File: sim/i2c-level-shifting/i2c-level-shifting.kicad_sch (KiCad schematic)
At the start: 13 parts, among them Q1 NX6008NBKW

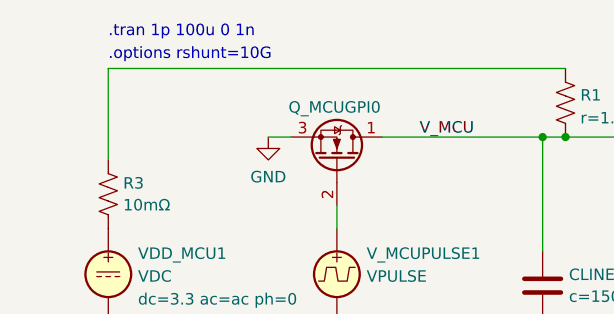
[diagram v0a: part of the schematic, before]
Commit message: More sane transient parameters.
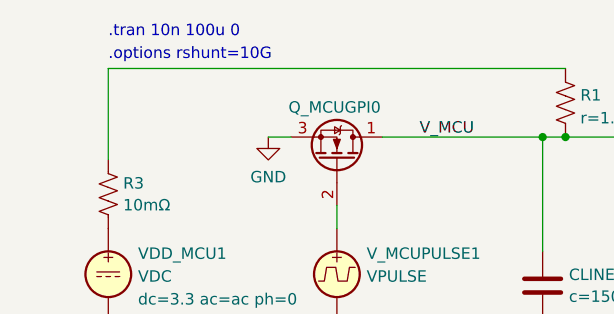
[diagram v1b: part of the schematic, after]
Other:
- note added: ".tran 10n 100u 0"
- note removed: ".tran 1p 100u 0 1n"
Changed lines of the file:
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@@
     (effects (font (size 1.27 1.27)) (justify left bottom))
   )
-  (text ".tran 1p 100u 0 1n" (at 76.2 123.698 0)
+  (text ".tran 10n 100u 0" (at 76.2 123.698 0)
     (effects (font (size 1.27 1.27)) (justify left bottom))
   )

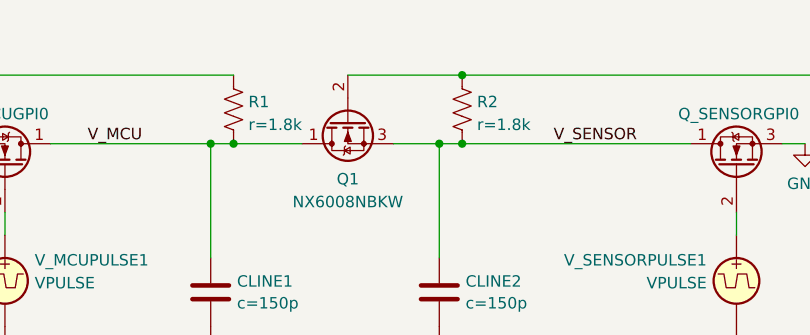
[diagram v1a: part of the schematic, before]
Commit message: Added gate resistors to reduce di/dt and thus supply noise.
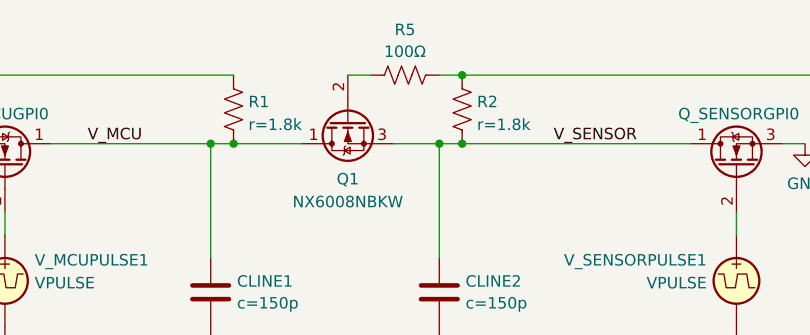
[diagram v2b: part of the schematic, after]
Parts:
- added R5: 100Ω, restall-generic-resistors:nominal-0402-1005, symbol restall-generic-resistors:resistor
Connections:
- net at R2.1, R4.1: now also R5.2; no longer Q1.2 (G)
- new net: Q1.2 (G), R5.1
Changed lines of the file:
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@@
     (stroke (width 0) (type default))
   )
-  (wire (pts (xy 139.7 127) (xy 152.4 127))
+  (wire (pts (xy 139.7 127) (xy 142.24 127))
     (stroke (width 0) (type default))
   )
@@
     (stroke (width 0) (type default))
   )
+  (wire (pts (xy 101.6 142.24) (xy 101.6 144.78))
+    (stroke (width 0) (type default))
+  )
   (wire (pts (xy 152.4 127) (xy 203.2 127))
     (stroke (width 0) (type default))
   )
-  (wire (pts (xy 101.6 142.24) (xy 101.6 144.78))
-    (stroke (width 0) (type default))
-  )
   (wire (pts (xy 124.46 134.62) (xy 124.46 147.32))
     (stroke (width 0) (type default))
   )
   (wire (pts (xy 73.66 193.04) (xy 68.58 193.04))
+    (stroke (width 0) (type default))
+  )
+  (wire (pts (xy 149.86 127) (xy 152.4 127))
     (stroke (width 0) (type default))
   )
@@
         )
       )
+    )
+  )
+  (symbol (lib_id "restall-generic-resistors:resistor") (at 146.05 127 90) (unit 1)
+    (in_bom yes) (on_board yes) (dnp no) (fields_autoplaced)
+    (property "Reference" "R5" (at 146.05 121.9667 90)
+      (effects (font (size 1.27 1.27)))
+    )
+    (property "Value" "100Ω" (at 146.05 124.3909 90)
+      (effects (font (size 1.27 1.27)))
+    )
+    (property "Footprint" "restall-generic-resistors:nominal-0402-1005" (at 146.304 125.984 90)
+      (effects (font (size 1.27 1.27)) (justify left) hide)
+    )
+    (property "Datasheet" "~" (at 146.05 127 0)
+      (effects (font (size 1.27 1.27)) (justify left) hide)
+    )
+    (property "Label" "???kΩ±1% ???W" (at 147.574 125.222 0)
+      (effects (font (size 1.27 1.27)) (justify left) hide)
+    )
+    (property "Tolerance" "±1%" (at 149.606 125.222 0)
+      (effects (font (size 1.27 1.27)) (justify left) hide)
+    )
+    (property "PowerRating" "0.0625W" (at 151.638 125.222 0)
+      (effects (font (size 1.27 1.27)) (justify left) hide)
+    )
+    (property "TemperatureCoefficient" "±100ppm" (at 153.67 125.222 0)
+      (effects (font (size 1.27 1.27)) (justify left) hide)
+    )
+    (property "Construction" "Thick Film" (at 155.702 125.222 0)
+      (effects (font (size 1.27 1.27)) (justify left) hide)
+    )
+    (property "Package" "0402" (at 157.734 125.222 0)
+      (effects (font (size 1.27 1.27)) (justify left) hide)
+    )
+    (property "Manufacturer" "" (at 146.05 127 0)
+      (effects (font (size 1.27 1.27)) (justify left) hide)
+    )
+    (property "ManufacturerPartNumber" "" (at 146.05 127 0)
+      (effects (font (size 1.27 1.27)) (justify left) hide)
+    )
+    (property "Manufacturer2" "" (at 146.05 127 0)
+      (effects (font (size 1.27 1.27)) (justify left) hide)
+    )
+    (property "Manufacturer2PartNumber" "" (at 146.05 127 0)
+      (effects (font (size 1.27 1.27)) (justify left) hide)
+    )
+    (property "Sim.Device" "R" (at 146.05 127 0)
+      (effects (font (size 1.27 1.27)) hide)
+    )
+    (property "Sim.Params" "r=100" (at 81.28 228.6 0)
+      (effects (font (size 1.27 1.27)) hide)
+    )
+    (property "Sim.Pins" "1=+ 2=-" (at 81.28 228.6 0)
+      (effects (font (size 1.27 1.27)) hide)
+    )
+    (pin "1")
+    (pin "2")
+    (instances
+      (project "i2c-level-shifting"
+        (path "/f5283a0e-9c80-4d21-8151-e5b7222edd6a"
+          (reference "R5") (unit 1)
+        )
+      )
